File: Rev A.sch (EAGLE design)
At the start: 86 parts, among them IC101 LM833N, IC102 LM833N, Q101 2N2907, Q102 2N2907, Q103 2N2222, Q104 2N2222, Q105 2N2222, Q106 2N2222, Q107 2N2907, Q108 2N2907, Q109 2N2222, Q110 2N2222, Q111 2N2222, Q112 2N2907, Q113 2N2222, Q114 2N2907, Q115 BD140, Q116 BD139, Q117 BD140, Q118 BD139

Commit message: Final schematic?
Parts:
- removed C102: 1uF, rcl:C-EU050-050X075
- removed C104: 4.7uF, rcl:CPOL-EUE2-5
- removed C207, C208: 1000uF, rcl:CPOL-EUE5-10.5
- removed IC101, IC102: LM833N, linear:LM833N
- removed L_IN, L_OUT, R_IN, R_OUT: (no value), adafruit:JST_2PIN-THM
- removed L_VOL, R_VOL: 100kΩ, bourns:3362U
- removed R123, R124: 1kΩ, rcl:R-EU_0207/10
- removed R125, R126, R127, R128: 0.33Ω, rcl:R-EU_0309/12
- added C103: 4.7uF, rcl:C-EU225-113X268
- added C105: 100pF, rcl:C-EU050-050X075
- added D109, D110, D111, D112: 1N4148DO35-7, diode:1N4148DO35-7
- added L_IN+, L_IN-, L_SPK+, L_SPK-, R_IN+, R_IN-, R_SPK+, R_SPK-: PIN2F061.100, con-faston:PIN2F061.100
- added Q119: BD140, transistor-power:BD140
- added Q120: BD139, transistor-power:BD139
- C101: value 1uF -> 4.7uF; device rcl:C-EU050-050X075 -> rcl:C-EU225-113X268
- C106: value 4.7uF -> 100pF; device rcl:CPOL-EUE2-5 -> rcl:C-EU050-050X075
- C107, C108: value 100pF -> 100n; device rcl:C-EU050-050X075 -> rcl:C-EU075-042X103
- C203, C204: value 100nF -> 2200uF; device rcl:C-EU025-025X050 -> rcl:CPOL-EUE5-10.5
- C205, C206: value 1000uF -> 2200uF
- KK101, KK102, KK103, KK104: value SK104-PAD -> SK129-PAD; device heatsink:SK104-PAD -> heatsink:SK129-PAD
- Q101, Q102, Q107, Q108, Q114: value 2N2907 -> 2N3906; device transistor-pnp:2N2907 -> transistor-pnp:2N3906
- Q103, Q104, Q105, Q106, Q110, Q113: value 2N2222 -> 2N3904; device transistor:2N2222 -> transistor-npn:2N3904
- Q109, Q111: value 2N2222 -> 2N3906; device transistor:2N2222 -> transistor-pnp:2N3906
- Q112: value 2N2907 -> 2N3904; device transistor-pnp:2N2907 -> transistor-npn:2N3904
- Q115: value BD140 -> 2N3904; device transistor-power:BD140 -> transistor-npn:2N3904
- Q116: value BD139 -> 2N3906; device transistor-power:BD139 -> transistor-pnp:2N3906
- R101, R102: value 47kΩ -> 10kΩ
- R103, R104: value 1.5kΩ -> 12kΩ
- R105, R106: value 15kΩ -> 10kΩ
- R109, R110: value 47kΩ -> 4.7kΩ
- R111, R112: value 10kΩ -> 560
- R113, R114: value 8.2kΩ -> 1kΩ
- R115, R116: value 10kΩ -> 1kΩ
- R117, R118: value 10kΩ -> 0.33Ω; device rcl:R-EU_0207/10 -> rcl:R-EU_0309/12
- R119, R120: value 2.7kΩ -> 0.33Ω; device rcl:R-EU_0207/10 -> rcl:R-EU_0309/12
- R121, R122: value 1kΩ -> 10Ω; device rcl:R-EU_0207/10 -> resistor-power:RMNS-5
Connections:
- removed net N$13 (its old number): L_VOL.3, R104.2
- removed net N$30: C106.+, IC102B.OUT, R110.2
- removed net N$56: IC101A.-IN, IC101A.OUT, R103.1
- removed net N$58: IC101B.+IN, R105.2, R_VOL.2
- removed net N$60: R103.2, R_VOL.3
- removed net N$62: IC101B.-IN, R107.2, R109.1
- removed net N$9 (its old number): C101.2, IC101A.+IN, R101.2
- new net N$17: C108.1, R122.1
- new net N$24: D105.C, D106.A
- new net N$35: D107.C, D108.A
- net GND: now also C107.2, C108.2, C203.+, C204.+, C205.-, C206.-, L_IN-.1, L_SPK-.1, R109.1, R110.1, R_IN-.1, R_SPK-.1; no longer C201.2, C202.2, C205.+, C206.+, C207.-, C208.-, L_IN.1, L_OUT.1, L_VOL.1, R107.1, R108.1, R111.1, R112.1, R115.1, R116.1, R_IN.1, R_OUT.1, R_VOL.1
- net L_OUT: now also D111.A, D112.C, L_SPK+.1, R108.2, R119.1, R120.2, R122.2; no longer D107.A, D108.C, L_OUT.2, R118.2, R127.1, R128.2
- net N$1: now also D105.A, Q109.C, Q113.B; no longer D101.A, Q111.B, R119.1
- net N$11: now also Q109.E, R111.1; no longer IC102A.-IN, IC102A.OUT, R104.1
- net N$12: now also D104.C, Q111.B, R110.2; no longer IC102B.+IN, L_VOL.2, R106.2
- net N$14: now also Q111.E, R112.1; no longer IC102B.-IN, R108.2, R110.1
- net N$15: now also C103.1, L_IN+.1; no longer C102.1, L_IN.2
- net N$16: now also C107.1, R121.1; no longer C102.2, IC102A.+IN, R102.2
- net N$2: now also R103.1; no longer R113.1
- net N$25: now also C103.2, R102.2; no longer C106.-, R112.2
- net N$26: now also Q113.C, Q117.B, R113.1; no longer Q111.C, Q115.B, R121.1
- net N$27: now also Q114.C, Q118.B, R114.2; no longer Q112.C, Q116.B, R122.2
- net N$28: now also Q114.E, Q118.C, R118.1; no longer Q112.E, Q116.C, R126.1
- net N$29: now also Q113.E, Q117.C, R117.2; no longer Q111.E, Q115.C, R125.2
- net N$31: now also C105.2, D106.C, Q110.C, Q114.B; no longer C107.2, D102.C, Q109.C, Q112.B
- net N$32: now also R105.2, R107.1; no longer R115.2, R117.1
- net N$33: now also R104.1; no longer R114.1
- net N$34: now also C106.1, Q112.B; no longer C108.1, Q110.B
- net N$36: now also D107.A, Q111.C, Q115.B; no longer D103.A, Q113.B, R120.1
- net N$37: now also Q115.C, Q119.B, R115.1; no longer Q113.C, Q117.B, R123.1
- net N$38: now also Q115.E, Q119.C, R119.2; no longer Q113.E, Q117.C, R127.2
- net N$39: now also Q116.C, Q120.B, R116.2; no longer Q114.C, Q118.B, R124.2
- net N$40: now also Q116.E, Q120.C, R120.1; no longer Q114.E, Q118.C, R128.1
- net N$41: now also C106.2, D108.C, Q112.C, Q116.B; no longer C108.2, D104.C, Q110.C, Q114.B
- net N$42: now also R106.2, R108.1; no longer R116.2, R118.1
- net N$5: now also C101.2, R101.2; no longer C104.-, R111.2
- net N$6: now also D102.C, Q109.B; no longer C104.+, IC101B.OUT
- net N$7: now also R_IN+.1; no longer R_IN.2
- net N$8: now also C105.1, Q110.B; no longer C107.1, Q109.B
- net R_OUT: now also D109.A, D110.C, R107.2, R117.1, R118.2, R121.2, R_SPK+.1; no longer D105.A, D106.C, R117.2, R125.1, R126.2, R_OUT.2
- net V+: now also C201.1, C205.+, C206.+, D101.A, D103.A, D109.C, D111.C, Q119.E, R103.2, R104.2, R111.2, R112.2, R115.2; no longer C203.1, C204.1, C207.+, C208.+, D105.C, D107.C, IC101P.V+, IC102P.V+, Q115.E, R114.2, R119.2, R120.2, R121.2, R123.2
- net V-: now also C201.2, C202.2, C203.-, C204.-, D110.A, D112.A, Q112.E, Q120.E, R114.1, R116.1; no longer C201.1, C203.2, C204.2, C205.-, C206.-, D106.A, D108.A, IC101P.V-, IC102P.V-, Q109.E, Q116.E, R122.1, R124.1
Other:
- moved on the sheet: C101, C107, C108, C201, C202, C205, C206, D101, D102, D103, D104, D105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

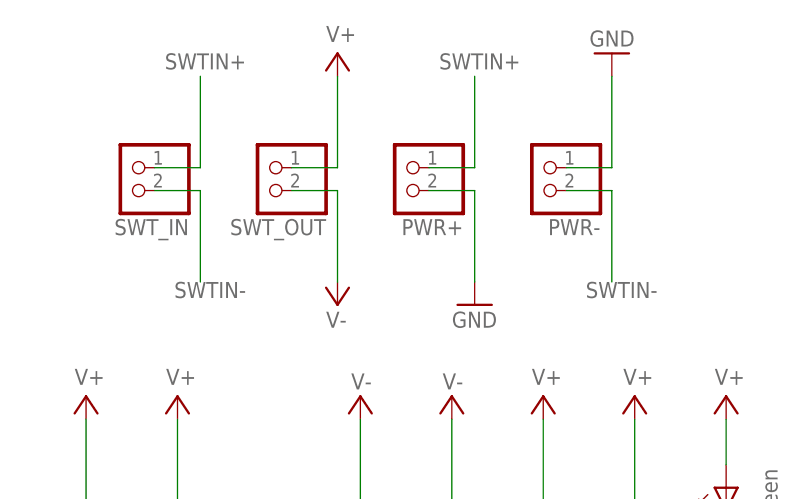
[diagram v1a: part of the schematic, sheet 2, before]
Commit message: Switched every JST connector to a Faston tab
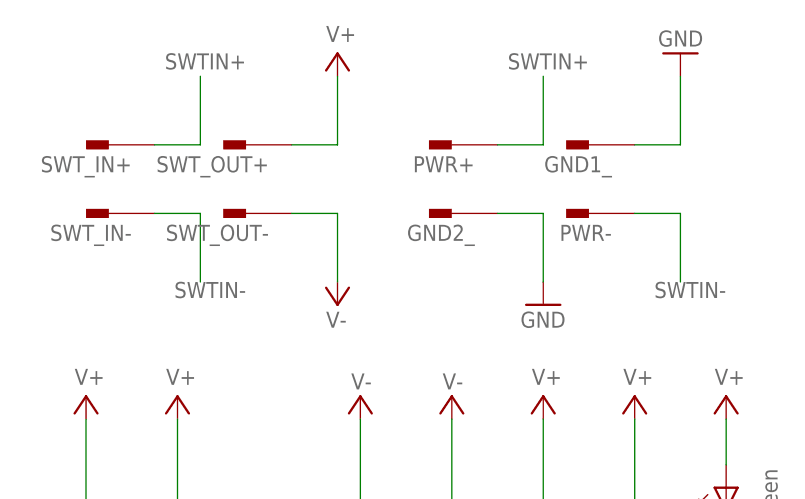
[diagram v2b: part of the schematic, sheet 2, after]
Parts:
- removed SWT_IN, SWT_OUT: (no value), adafruit:JST_2PIN-THM
- added GND1_, GND2_, SWT_IN+, SWT_IN-, SWT_OUT+, SWT_OUT-: PIN2F061.100, con-faston:PIN2F061.100
- PWR+, PWR-: value (none) -> PIN2F061.100; device adafruit:JST_2PIN-THM -> con-faston:PIN2F061.100
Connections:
- net GND: now also GND1_.1, GND2_.1; no longer PWR+.1, PWR-.2
- net SWTIN+: now also PWR+.1, SWT_IN+.1; no longer PWR+.2, SWT_IN.2
- net SWTIN-: now also SWT_IN-.1; no longer SWT_IN.1
- net V+: now also SWT_OUT+.1; no longer SWT_OUT.2
- net V-: now also SWT_OUT-.1; no longer SWT_OUT.1
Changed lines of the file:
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@@
 <part name="C205" library="rcl" deviceset="CPOL-EU" device="E5-10.5" value="2200uF"/>
 <part name="C203" library="rcl" deviceset="CPOL-EU" device="E5-10.5" value="2200uF"/>
-<part name="PWR+" library="adafruit" deviceset="JST_2PIN" device="-THM"/>
-<part name="PWR-" library="adafruit" deviceset="JST_2PIN" device="-THM"/>
-<part name="SWT_OUT" library="adafruit" deviceset="JST_2PIN" device="-THM"/>
-<part name="SWT_IN" library="adafruit" deviceset="JST_2PIN" device="-THM"/>
 <part name="SUPPLY60" library="supply2" deviceset="V-" device=""/>
 <part name="SUPPLY7" library="supply2" deviceset="V-" device=""/>
@@
 <part name="L_SPK+" library="con-faston" deviceset="PIN2" device="F061.100"/>
 <part name="L_SPK-" library="con-faston" deviceset="PIN2" device="F061.100"/>
+<part name="SWT_IN+" library="con-faston" deviceset="PIN2" device="F061.100"/>
+<part name="SWT_IN-" library="con-faston" deviceset="PIN2" device="F061.100"/>
+<part name="SWT_OUT+" library="con-faston" deviceset="PIN2" device="F061.100"/>
+<part name="SWT_OUT-" library="con-faston" deviceset="PIN2" device="F061.100"/>
+<part name="PWR+" library="con-faston" deviceset="PIN2" device="F061.100"/>
+<part name="GND2_" library="con-faston" deviceset="PIN2" device="F061.100"/>
+<part name="GND1_" library="con-faston" deviceset="PIN2" device="F061.100"/>
+<part name="PWR-" library="con-faston" deviceset="PIN2" device="F061.100"/>
 </parts>
 <sheets>
@@
 <instance part="C205" gate="G$1" x="55.88" y="33.02"/>
 <instance part="C203" gate="G$1" x="35.56" y="30.48" rot="R180"/>
-<instance part="PWR+" gate="G$1" x="40.64" y="76.2" rot="R180"/>
-<instance part="PWR-" gate="G$1" x="55.88" y="76.2" rot="R180"/>
-<instance part="SWT_OUT" gate="G$1" x="25.4" y="76.2" rot="R180"/>
-<instance part="SWT_IN" gate="G$1" x="10.16" y="76.2" rot="R180"/>
 <instance part="SUPPLY60" gate="1" x="76.2" y="12.7"/>
 <instance part="SUPPLY7" gate="1" x="33.02" y="60.96"/>
-<instance part="GND3" gate="1" x="48.26" y="60.96"/>
-<instance part="GND6" gate="1" x="63.5" y="88.9" rot="R180"/>
+<instance part="GND3" gate="1" x="55.88" y="60.96"/>
+<instance part="GND6" gate="1" x="71.12" y="88.9" rot="R180"/>
 <instance part="C202" gate="G$1" x="15.24" y="33.02"/>
 <instance part="SUPPLY11" gate="1" x="15.24" y="50.8"/>
@@
 <instance part="C204" gate="G$1" x="45.72" y="30.48" rot="R180"/>
 <instance part="ON" gate="G$1" x="76.2" y="40.64"/>
+<instance part="SWT_IN+" gate="-1" x="7.62" y="78.74" smashed="yes" rot="R180">
+<attribute name="NAME" x="10.16" y="77.47" size="1.778" layer="95" rot="R180"/>
+</instance>
+<instance part="SWT_IN-" gate="-1" x="7.62" y="71.12" smashed="yes" rot="R180">
+<attribute name="NAME" x="10.16" y="69.85" size="1.778" layer="95" rot="R180"/>
+</instance>
+<instance part="SWT_OUT+" gate="-1" x="22.86" y="78.74" smashed="yes" rot="R180">
+<attribute name="NAME" x="25.4" y="77.47" size="1.778" layer="95" rot="R180"/>
+</instance>
+<instance part="SWT_OUT-" gate="-1" x="22.86" y="71.12" smashed="yes" rot="R180">
+<attribute name="NAME" x="25.4" y="69.85" size="1.778" layer="95" rot="R180"/>
+</instance>
+<instance part="PWR+" gate="-1" x="45.72" y="78.74" smashed="yes" rot="R180">
+<attribute name="NAME" x="48.26" y="77.47" size="1.778" layer="95" rot="R180"/>
+</instance>
+<instance part="GND2_" gate="-1" x="45.72" y="71.12" smashed="yes" rot="R180">
+<attribute name="NAME" x="48.26" y="69.85" size="1.778" layer="95" rot="R180"/>
+</instance>
+<instance part="GND1_" gate="-1" x="60.96" y="78.74" smashed="yes" rot="R180">
+<attribute name="NAME" x="63.5" y="77.47" size="1.778" layer="95" rot="R180"/>
+</instance>
+<instance part="PWR-" gate="-1" x="60.96" y="71.12" smashed="yes" rot="R180">
+<attribute name="NAME" x="63.5" y="69.85" size="1.778" layer="95" rot="R180"/>
+</instance>
 </instances>
 <busses>
@@
 </segment>
 <segment>
-<pinref part="PWR+" gate="G$1" pin="1"/>
-<wire x1="43.18" y1="73.66" x2="48.26" y2="73.66" width="0.1524" layer="91"/>
+<wire x1="50.8" y1="71.12" x2="55.88" y2="71.12" width="0.1524" layer="91"/>
 <pinref part="GND3" gate="1" pin="GND"/>
-<wire x1="48.26" y1="73.66" x2="48.26" y2="63.5" width="0.1524" layer="91"/>
-</segment>
-<segment>
-<pinref part="PWR-" gate="G$1" pin="2"/>
-<wire x1="58.42" y1="76.2" x2="63.5" y2="76.2" width="0.1524" layer="91"/>
-<wire x1="63.5" y1="76.2" x2="63.5" y2="86.36" width="0.1524" layer="91"/>
+<wire x1="55.88" y1="71.12" x2="55.88" y2="63.5" width="0.1524" layer="91"/>
+<pinref part="GND2_" gate="-1" pin="1"/>
+</segment>
+<segment>
+<wire x1="66.04" y1="78.74" x2="71.12" y2="78.74" width="0.1524" layer="91"/>
+<wire x1="71.12" y1="78.74" x2="71.12" y2="86.36" width="0.1524" layer="91"/>
 <pinref part="GND6" gate="1" pin="GND"/>
+<pinref part="GND1_" gate="-1" pin="1"/>
 </segment>
 <segment>
@@
 </segment>
 <segment>
-<pinref part="SWT_OUT" gate="G$1" pin="1"/>
-<wire x1="33.02" y1="73.66" x2="27.94" y2="73.66" width="0.1524" layer="91"/>
+<wire x1="33.02" y1="71.12" x2="27.94" y2="71.12" width="0.1524" layer="91"/>
 <pinref part="SUPPLY7" gate="1" pin="V-"/>
-<wire x1="33.02" y1="63.5" x2="33.02" y2="73.66" width="0.1524" layer="91"/>
+<wire x1="33.02" y1="63.5" x2="33.02" y2="71.12" width="0.1524" layer="91"/>
+<pinref part="SWT_OUT-" gate="-1" pin="1"/>
 </segment>
 <segment>
@@
 <segment>
 <pinref part="SUPPLY58" gate="1" pin="V+"/>
-<wire x1="33.02" y1="76.2" x2="33.02" y2="86.36" width="0.1524" layer="91"/>
-<pinref part="SWT_OUT" gate="G$1" pin="2"/>
-<wire x1="27.94" y1="76.2" x2="33.02" y2="76.2" width="0.1524" layer="91"/>
+<wire x1="33.02" y1="78.74" x2="33.02" y2="86.36" width="0.1524" layer="91"/>
+<wire x1="27.94" y1="78.74" x2="33.02" y2="78.74" width="0.1524" layer="91"/>
+<pinref part="SWT_OUT+" gate="-1" pin="1"/>
 </segment>
 <segment>
@@
 <net name="SWTIN+" class="0">
 <segment>
-<pinref part="SWT_IN" gate="G$1" pin="2"/>
-<wire x1="12.7" y1="76.2" x2="17.78" y2="76.2" width="0.1524" layer="91"/>
-<wire x1="17.78" y1="76.2" x2="17.78" y2="86.36" width="0.1524" layer="91"/>
+<wire x1="12.7" y1="78.74" x2="17.78" y2="78.74" width="0.1524" layer="91"/>
+<wire x1="17.78" y1="78.74" x2="17.78" y2="86.36" width="0.1524" layer="91"/>
 <label x="22.86" y="88.9" size="1.778" layer="95" rot="R180"/>
-</segment>
-<segment>
-<pinref part="PWR+" gate="G$1" pin="2"/>
-<wire x1="48.26" y1="76.2" x2="43.18" y2="76.2" width="0.1524" layer="91"/>
-<wire x1="48.26" y1="76.2" x2="48.26" y2="86.36" width="0.1524" layer="91"/>
-<label x="53.34" y="88.9" size="1.778" layer="95" rot="R180"/>
+<pinref part="SWT_IN+" gate="-1" pin="1"/>
+</segment>
+<segment>
+<wire x1="55.88" y1="78.74" x2="50.8" y2="78.74" width="0.1524" layer="91"/>
+<wire x1="55.88" y1="78.74" x2="55.88" y2="86.36" width="0.1524" layer="91"/>
+<label x="60.96" y="88.9" size="1.778" layer="95" rot="R180"/>
+<pinref part="PWR+" gate="-1" pin="1"/>
 </segment>
 </net>
 <net name="SWTIN-" class="0">
 <segment>
-<pinref part="SWT_IN" gate="G$1" pin="1"/>
-<wire x1="12.7" y1="73.66" x2="17.78" y2="73.66" width="0.1524" layer="91"/>
-<wire x1="17.78" y1="73.66" x2="17.78" y2="63.5" width="0.1524" layer="91"/>
+<wire x1="12.7" y1="71.12" x2="17.78" y2="71.12" width="0.1524" layer="91"/>
+<wire x1="17.78" y1="71.12" x2="17.78" y2="63.5" width="0.1524" layer="91"/>
 <label x="22.86" y="63.5" size="1.778" layer="95" rot="R180"/>
-</segment>
-<segment>
-<pinref part="PWR-" gate="G$1" pin="1"/>
-<wire x1="58.42" y1="73.66" x2="63.5" y2="73.66" width="0.1524" layer="91"/>
-<wire x1="63.5" y1="73.66" x2="63.5" y2="63.5" width="0.1524" layer="91"/>
-<label x="68.58" y="63.5" size="1.778" layer="95" rot="R180"/>
-</segment>
-</net>
+<pinref part="SWT_IN-" gate="-1" pin="1"/>
+</segment>
+<segment>
+<wire x1="66.04" y1="71.12" x2="71.12" y2="71.12" width="0.1524" layer="91"/>
+<wire x1="71.12" y1="71.12" x2="71.12" y2="63.5" width="0.1524" layer="91"/>
+<label x="76.2" y="63.5" size="1.778" layer="95" rot="R180"/>
+<pinref part="PWR-" gate="-1" pin="1"/>
+</segment>
+</net>
